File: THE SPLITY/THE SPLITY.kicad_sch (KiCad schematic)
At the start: 59 parts, among them U2 Nice_Nano_V2

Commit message: added a battery connector
boo
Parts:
- added J1: Conn_01x02_Socket, Connector_JST:JST_XH_B2B-XH-AM_1x02_P2.50mm_Vertical, symbol Connector:Conn_01x02_Socket
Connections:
- net -: now reaches U2.23 (GND)
- net -: now also J1.2 (Pin_2)
- net +: now reaches U2.24 (B+)
- net +: now also J1.1 (Pin_1)
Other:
- moved on the sheet: U2
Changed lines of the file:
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@@
 	(global_label "column 5"
 		(shape input)
-		(at 57.15 114.3 180)
+		(at 78.74 110.49 180)
 		(fields_autoplaced yes)
 		(effects
@@
 		)
 		(property "Intersheetrefs" "${INTERSHEET_REFS}"
-			(at 45.0936 114.3 0)
+			(at 66.6836 110.49 0)
 			(effects
 				(font
@@
 	(global_label "row 0"
 		(shape input)
-		(at 87.63 109.22 0)
+		(at 109.22 105.41 0)
 		(fields_autoplaced yes)
 		(effects
@@
 		)
 		(property "Intersheetrefs" "${INTERSHEET_REFS}"
-			(at 96.058 109.22 0)
+			(at 117.648 105.41 0)
 			(effects
 				(font
@@
 	(global_label "column 3"
 		(shape input)
-		(at 57.15 109.22 180)
+		(at 78.74 105.41 180)
 		(fields_autoplaced yes)
 		(effects
@@
 		)
 		(property "Intersheetrefs" "${INTERSHEET_REFS}"
-			(at 45.0936 109.22 0)
+			(at 66.6836 105.41 0)
 			(effects
 				(font
@@
 	(global_label "column 4"
 		(shape input)
-		(at 57.15 111.76 180)
+		(at 78.74 107.95 180)
 		(fields_autoplaced yes)
 		(effects
@@
 		)
 		(property "Intersheetrefs" "${INTERSHEET_REFS}"
-			(at 45.0936 111.76 0)
+			(at 66.6836 107.95 0)
 			(effects
 				(font
@@
 		)
 	)
+	(global_label "-"
+		(shape input)
+		(at 109.22 90.17 0)
+		(fields_autoplaced yes)
+		(effects
+			(font
+				(size 1.27 1.27)
+			)
+			(justify left)
+		)
+		(property "Intersheetrefs" "${INTERSHEET_REFS}"
+			(at 113.7776 90.17 0)
+			(effects
+				(font
+					(size 1.27 1.27)
+				)
+				(justify left)
+				(hide yes)
+			)
+		)
+	)
 	(global_label "column 1"
 		(shape input)
-		(at 57.15 104.14 180)
+		(at 78.74 100.33 180)
+		(fields_autoplaced yes)
+		(effects
+			(font
+				(size 1.27 1.27)
+			)
+			(justify right)
+		)
+		(property "Intersheetrefs" "${INTERSHEET_REFS}"
+			(at 66.6836 100.33 0)
+			(effects
+				(font
+					(size 1.27 1.27)
+				)
+				(justify right)
+				(hide yes)
+			)
+		)
+	)
+	(global_label "-"
+		(shape input)
+		(at 114.3 76.2 180)
 		(fields_autoplaced yes)
 		(effects
@@
 		)
 		(property "Intersheetrefs" "${INTERSHEET_REFS}"
-			(at 45.0936 104.14 0)
+			(at 109.7424 76.2 0)
 			(effects
 				(font
@@
 	(global_label "row 3"
 		(shape input)
-		(at 87.63 116.84 0)
+		(at 109.22 113.03 0)
 		(fields_autoplaced yes)
 		(effects
@@
 		)
 		(property "Intersheetrefs" "${INTERSHEET_REFS}"
-			(at 96.058 116.84 0)
+			(at 117.648 113.03 0)
 			(effects
 				(font
@@
 		)
 	)
+	(global_label "+"
+		(shape input)
+		(at 114.3 73.66 180)
+		(fields_autoplaced yes)
+		(effects
+			(font
+				(size 1.27 1.27)
+			)
+			(justify right)
+		)
+		(property "Intersheetrefs" "${INTERSHEET_REFS}"
+			(at 109.7424 73.66 0)
+			(effects
+				(font
+					(size 1.27 1.27)
+				)
+				(justify right)
+				(hide yes)
+			)
+		)
+	)
 	(global_label "column 0"
 		(shape input)
@@
 	(global_label "row 1"
 		(shape input)
-		(at 87.63 111.76 0)
+		(at 109.22 107.95 0)
 		(fields_autoplaced yes)
 		(effects
@@
 		)
 		(property "Intersheetrefs" "${INTERSHEET_REFS}"
-			(at 96.058 111.76 0)
+			(at 117.648 107.95 0)
+			(effects
+				(font
+					(size 1.27 1.27)
+				)
+				(justify left)
+				(hide yes)
+			)
+		)
+	)
+	(global_label "+"
+		(shape input)
+		(at 109.22 87.63 0)
+		(fields_autoplaced yes)
+		(effects
+			(font
+				(size 1.27 1.27)
+			)
+			(justify left)
+		)
+		(property "Intersheetrefs" "${INTERSHEET_REFS}"
+			(at 113.7776 87.63 0)
 			(effects
 				(font
@@
 	(global_label "row 2"
 		(shape input)
-		(at 87.63 114.3 0)
+		(at 109.22 110.49 0)
 		(fields_autoplaced yes)
 		(effects
@@
 		)
 		(property "Intersheetrefs" "${INTERSHEET_REFS}"
-			(at 96.058 114.3 0)
+			(at 117.648 110.49 0)
 			(effects
 				(font
@@
 	(global_label "column 2"
 		(shape input)
-		(at 57.15 106.68 180)
+		(at 78.74 102.87 180)
 		(fields_autoplaced yes)
 		(effects
@@
 		)
 		(property "Intersheetrefs" "${INTERSHEET_REFS}"
-			(at 45.0936 106.68 0)
+			(at 66.6836 102.87 0)
 			(effects
 				(font
@@
 	(global_label "row 4"
 		(shape input)
-		(at 87.63 119.38 0)
+		(at 109.22 115.57 0)
 		(fields_autoplaced yes)
 		(effects
@@
 		)
 		(property "Intersheetrefs" "${INTERSHEET_REFS}"
-			(at 96.058 119.38 0)
+			(at 117.648 115.57 0)
 			(effects
 				(font
@@
 	(global_label "column 0"
 		(shape input)
-		(at 57.15 101.6 180)
+		(at 78.74 97.79 180)
 		(fields_autoplaced yes)
 		(effects
@@
 		)
 		(property "Intersheetrefs" "${INTERSHEET_REFS}"
-			(at 45.0936 101.6 0)
+			(at 66.6836 97.79 0)
 			(effects
 				(font
@@
 	(symbol
 		(lib_id "ScottoKeebs:MCU_Nice_Nano_V2")
-		(at 72.39 105.41 0)
+		(at 93.98 101.6 0)
 		(unit 1)
 		(exclude_from_sim no)
@@
 		(dnp no)
 		(property "Reference" "U2"
-			(at 72.39 124.46 0)
+			(at 93.98 120.65 0)
 			(effects
 				(font
@@
 		)
 		(property "Value" "Nice_Nano_V2"
-			(at 72.39 127 0)
+			(at 93.98 123.19 0)
 			(effects
 				(font
@@
 		)
 		(property "Footprint" "ScottoKeebs_MCU:Nice_Nano_V2_Flipped"
-			(at 72.39 128.27 0)
+			(at 93.98 124.46 0)
 			(effects
 				(font
@@
 		)
 		(property "Datasheet" ""
-			(at 99.06 168.91 90)
+			(at 120.65 165.1 90)
 			(effects
 				(font
@@
 		)
 		(property "Description" ""
-			(at 72.39 105.41 0)
+			(at 93.98 101.6 0)
 			(effects
 				(font
@@
 					(unit 1)
 				)
+			)
+		)
+	)
+	(symbol
+		(lib_id "Connector:Conn_01x02_Socket")
+		(at 119.38 73.66 0)
+		(unit 1)
+		(exclude_from_sim no)
+		(in_bom yes)
+		(on_board yes)
+		(dnp no)
+		(fields_autoplaced yes)
+		(property "Reference" "J1"
+			(at 120.65 73.6599 0)
+			(effects
+				(font
+					(size 1.27 1.27)
+				)
+				(justify left)
+			)
+		)
+		(property "Value" "Conn_01x02_Socket"
+			(at 120.65 76.1999 0)
+			(effects
+				(font
+					(size 1.27 1.27)
+				)
+				(justify left)
+			)
+		)
+		(property "Footprint" "Connector_JST:JST_XH_B2B-XH-AM_1x02_P2.50mm_Vertical"
+			(at 119.38 73.66 0)
+			(effects
+				(font
+					(size 1.27 1.27)
+				)
+				(hide yes)
+			)
+		)
+		(property "Datasheet" "~"
+			(at 119.38 73.66 0)
+			(effects
+				(font
+					(size 1.27 1.27)
+				)
+				(hide yes)
+			)
+		)
+		(property "Description" "Generic connector, single row, 01x02, script generated"
+			(at 119.38 73.66 0)
+			(effects
+				(font
+					(size 1.27 1.27)
+				)
+				(hide yes)
+			)
+		)
+		(pin "1"
+		)
+		(pin "2"
+		)
+		(instances
+			(project ""
+				(path "/d377bd6e-6f97-4d3e-8a43-76ce85113ab3"
+					(reference "J1")
+					(unit 1)
+				)

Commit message: ז
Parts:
- added SW1, SW2: Switch, symbol ScottoKeebs:Placeholder_Switch
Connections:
- net -: now also SW1.2; no longer U2.23 (GND)
- net RST: now reaches U2.22 (RST)
- net RST: now also SW2.2
- new net GND: SW1.1, SW2.1, U2.23 (GND)

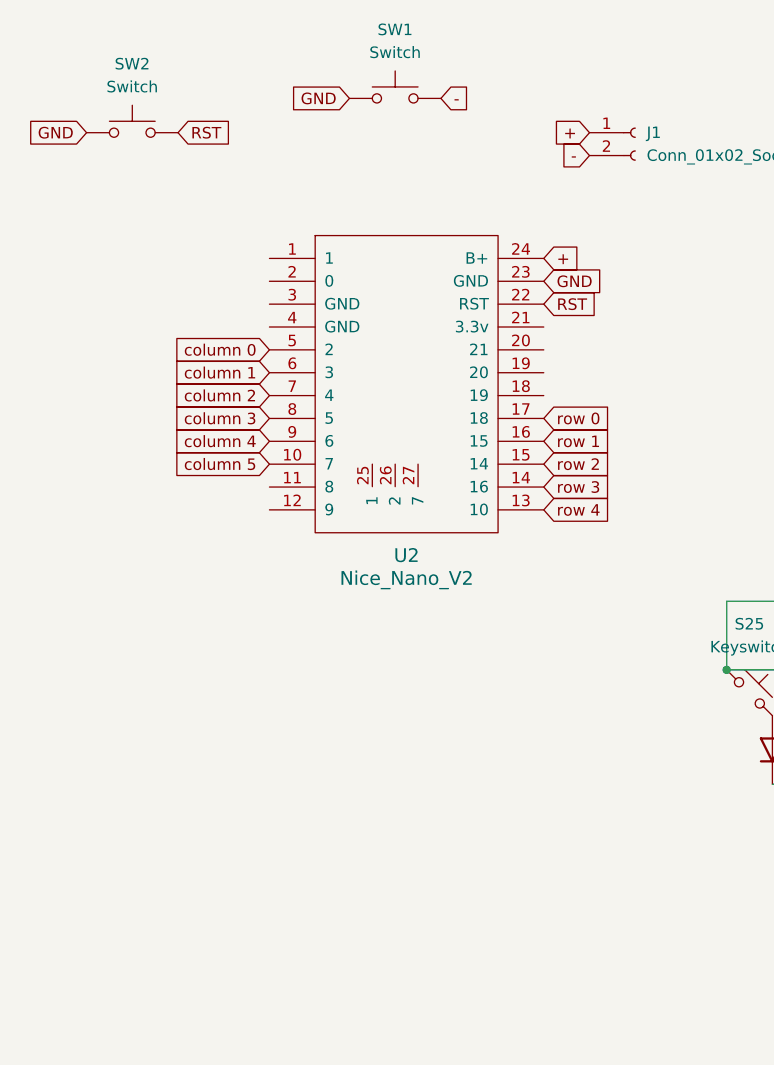
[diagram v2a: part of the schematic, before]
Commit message: mounting holes and outline change
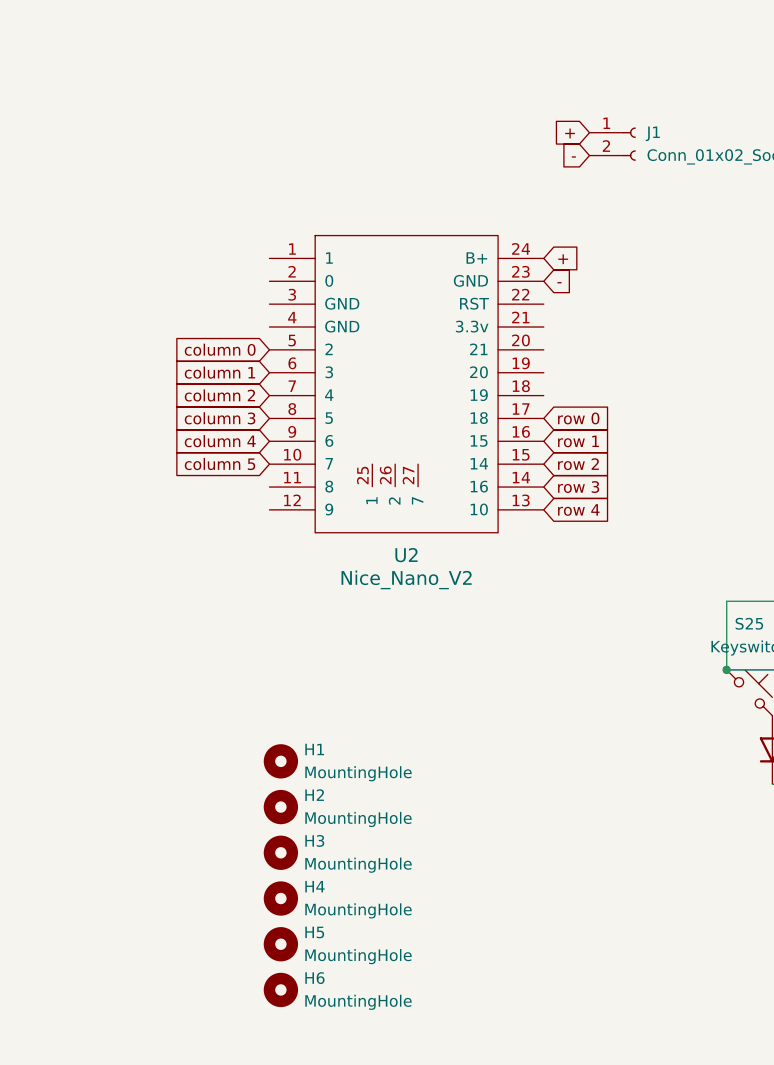
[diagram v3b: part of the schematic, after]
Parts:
- removed SW1, SW2: Switch, symbol ScottoKeebs:Placeholder_Switch
- added H1, H2, H3, H4, H5, H6: MountingHole, MountingHole:MountingHole_2.2mm_M2, symbol Mechanical:MountingHole
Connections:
- net GND is gone; now on net -: U2.23 (GND)
- net RST: no longer names the net of U2.22 (RST)

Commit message: updated some stuff
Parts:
- added D30, D31, D32, D33, D34, D35, D36, D37, D38, D39, D40, D41, D42, D43, D44, D45, D46, D47, D48, D49, D50, D51, D52, D53, D54, D55, D56, D57, D58: Diode, ScottoKeebs_Components:Diode_DO-35, symbol ScottoKeebs:Placeholder_Diode
- added H10, H11, H12, H7, H8, H9: MountingHole, MountingHole:MountingHole_2.2mm_M2, symbol Mechanical:MountingHole
- added J2: Conn_01x02_Socket, Connector_JST:JST_XH_B2B-XH-AM_1x02_P2.50mm_Vertical, symbol Connector:Conn_01x02_Socket
- added S30, S31, S32, S33, S34, S35, S36, S37, S38, S39, S40, S41, S42, S43, S44, S45, S46, S47, S48, S49, S50, S51, S52, S53, S54, S55, S56, S57, S58: Keyswitch, ScottoKeebs_MX:MX_PCB_1.00u, symbol ScottoKeebs:Placeholder_Keyswitch
- added U1: Nice_Nano_V2, ScottoKeebs_MCU:Nice_Nano_V2_Flipped, symbol ScottoKeebs:MCU_Nice_Nano_V2
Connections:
- new net: D35.2 (A), S35.2
- new net: D58.2 (A), S58.2
- new net: D57.2 (A), S57.2
- new net: D46.2 (A), S46.2
- new net: D37.2 (A), S37.2
- new net: D40.2 (A), S40.2
- new net: D45.2 (A), S45.2
- new net: D49.2 (A), S49.2
- new net: D33.2 (A), S33.2
- new net: D42.2 (A), S42.2
- new net: D34.2 (A), S34.2
- new net: D55.2 (A), S55.2
- new net: D43.2 (A), S43.2
- new net: D32.2 (A), S32.2
- new net: D47.2 (A), S47.2
- new net: D44.2 (A), S44.2
- new net: D30.2 (A), S30.2
- new net: D53.2 (A), S53.2
- new net: D36.2 (A), S36.2
- new net: D39.2 (A), S39.2
- new net: D50.2 (A), S50.2
- new net: D51.2 (A), S51.2
- new net: D48.2 (A), S48.2
- new net: D56.2 (A), S56.2
- new net: D38.2 (A), S38.2
- new net: D41.2 (A), S41.2
- new net: D54.2 (A), S54.2
- new net: D52.2 (A), S52.2
- new net: D31.2 (A), S31.2
- new net +.: J2.1 (Pin_1), U1.1
- new net -.: J2.2 (Pin_2), U1.2 (0)
- new net column 0.: S30.1, S31.1, S32.1, S33.1, S34.1, S35.1, U1.20 (21)
- new net column 1.: S36.1, S37.1, S38.1, S39.1, U1.19 (20)
- new net column 2.: S40.1, S41.1, S42.1, S43.1, S44.1, U1.18 (19)
- new net column 3.: S45.1, S46.1, S47.1, S48.1, S49.1, U1.17 (18)
- new net column 4.: S50.1, S51.1, S52.1, S53.1, S54.1, U1.16 (15)
- new net column 5.: S55.1, S56.1, S57.1, S58.1, U1.15 (14)
- new net row 0.: D32.1 (K), D36.1 (K), D41.1 (K), D46.1 (K), D51.1 (K), D55.1 (K), U1.8 (5)
- new net row 1.: D33.1 (K), D37.1 (K), D42.1 (K), D47.1 (K), D52.1 (K), D56.1 (K), U1.9 (6)
- new net row 2.: D30.1 (K), D34.1 (K), D38.1 (K), D43.1 (K), D48.1 (K), D53.1 (K), D57.1 (K), U1.10 (7)
- new net row 3.: D35.1 (K), D39.1 (K), D44.1 (K), D49.1 (K), D54.1 (K), D58.1 (K), U1.11 (8)
- new net row 4.: D31.1 (K), D40.1 (K), D45.1 (K), D50.1 (K), U1.12 (9)
